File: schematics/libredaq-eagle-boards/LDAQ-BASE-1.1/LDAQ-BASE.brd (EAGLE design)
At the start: 125 x 90.2 mm, 94 parts, among them J1 4840.2211, J2 M50-3610542, T1 FDN340P, U1 ATSAM3U1CB, U2 LM3671MF-3.3, U3 TS30012-M050QFNR, U4 ISL3175, U5 LMV321, U6 TXB0108PWR, Y1 12M

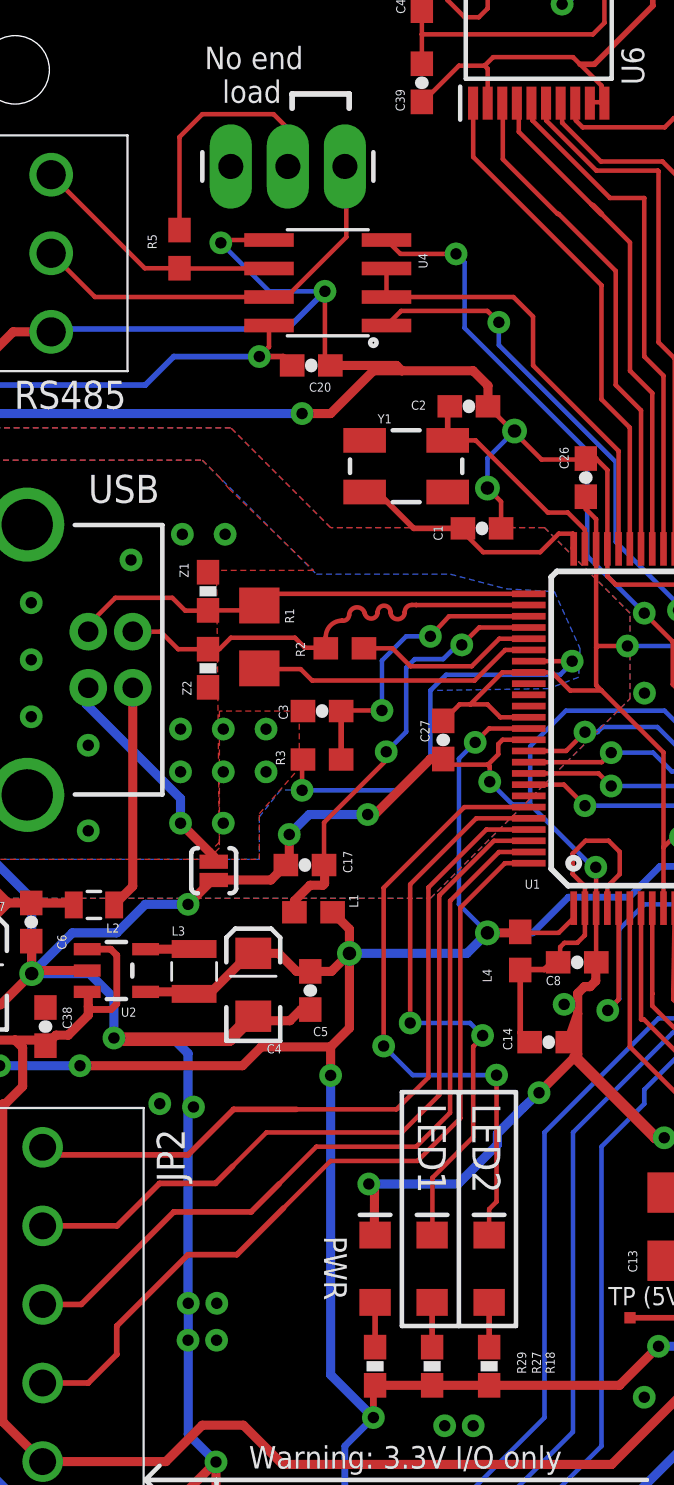
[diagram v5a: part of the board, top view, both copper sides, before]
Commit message: more missing components in circuithub
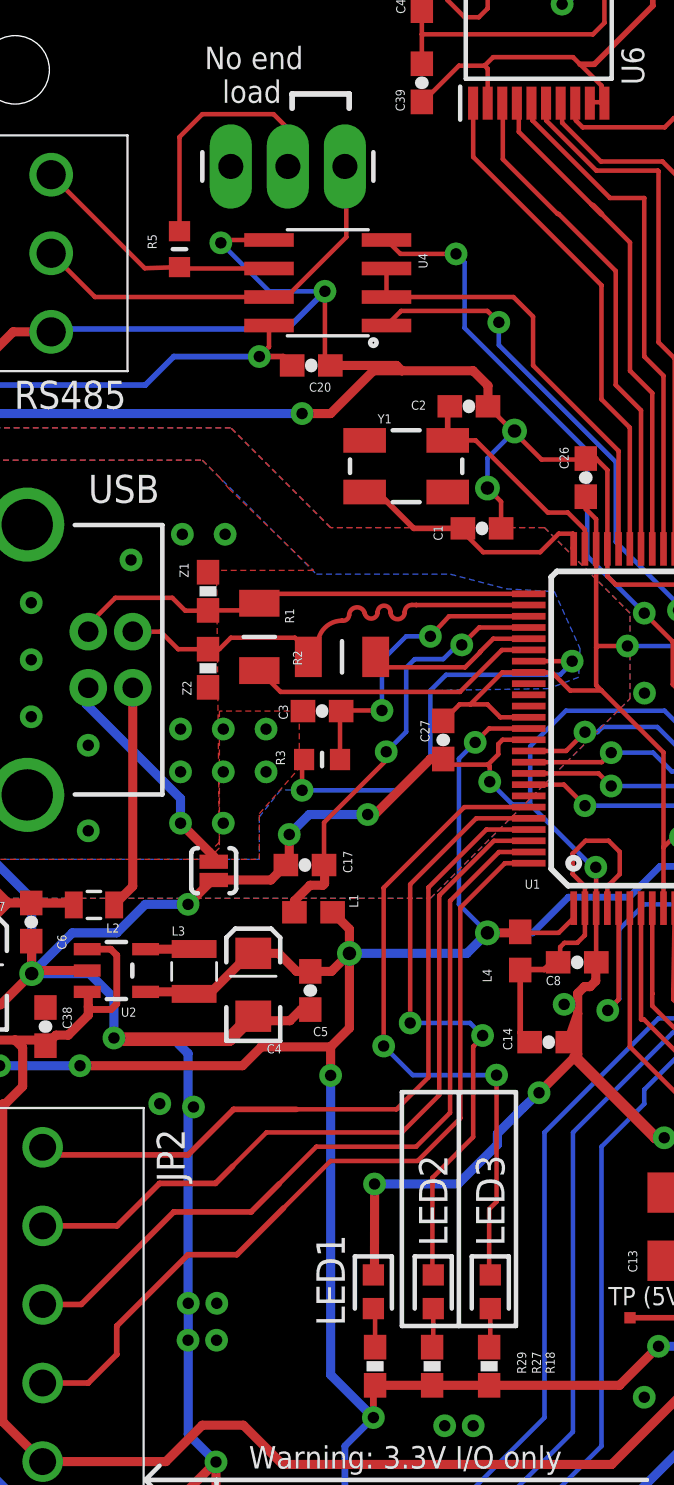
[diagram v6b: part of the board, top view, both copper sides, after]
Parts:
- removed PWR: BLUE, SparkFun-LED:LED-1206
- added LED3: 150060RS75000, SamacSys_Parts:LEDC1608X80N
- LED1: value RED -> 150060BS75000; device SparkFun-LED:LED-1206 -> SamacSys_Parts:LEDC1608X80N
- LED2: value RED -> 150060RS75000; device SparkFun-LED:LED-1206 -> SamacSys_Parts:LEDC1608X80N
- R1: value (none) -> CR1206-FX-39R0ELF; device SparkFun-Resistors:1206 -> SamacSys_Parts:RESC3216X75N
- R2: value (none) -> CR1206-FX-39R0ELF; device SparkFun-Resistors:0603 -> SamacSys_Parts:RESC3216X75N
- R3: value (none) -> SFR03EZPF6801; device SparkFun-Resistors:0603 -> SamacSys_Parts:RESC1608X55N
- R5: value (none) -> CRCW0603120RFKEAC; device SparkFun-Resistors:0603 -> SamacSys_Parts:RESC1608X55N
- moved LED1 2.81 mm to (21.0, 20.6), turned to 270 degrees
- moved LED2 2.69 mm to (23.6, 20.6), turned to 270 degrees
- moved R2 0.40 mm to (19.6, 48.9)
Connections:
- removed net N$33: PWR.A, R29.2
- new net N$16: LED1.2, R29.2
- net !LED1: now also LED2.1; no longer LED1.C
- net !LED2: now also LED3.1; no longer LED2.C
- net GND: now also LED1.1; no longer PWR.C
- net N$31: now also LED2.2; no longer LED1.A
- net N$32: now also LED3.2; no longer LED2.A
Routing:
- net N$33: track 1.99 -> 0.00 mm
- net !LED2: track 27.8 -> 29.6 mm
- net !LED1: track 26.0 -> 27.7 mm
- net N$16: track 0.00 -> 1.75 mm
- net GND: track 901.6 -> 903.0 mm
- net N$4: track 8.18 -> 7.55 mm
